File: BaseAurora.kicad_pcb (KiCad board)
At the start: 2 copper layers, 69.5 x 100 mm, 42 parts, among them J1 Conn_01x04_Male, J10 Conn_01x03_Male, J11 Screw_Terminal_01x02, J2 Conn_01x05_Male, J3 Screw_Terminal_01x02, J4 Conn_01x04_Male, J5 Conn_01x04_Male, J6 Screw_Terminal_01x02, J7 Screw_Terminal_01x02, J8 Header_1x2, J9 Header_1x2, K1 HK4100F-DC3V-SHG, Q1 2N3906, Q2 PN2222A, U1 ME6217C33M5G, U2 E32-915T20D, U3 4N32M, U4 NodeMCU1.0(ESP-12E)

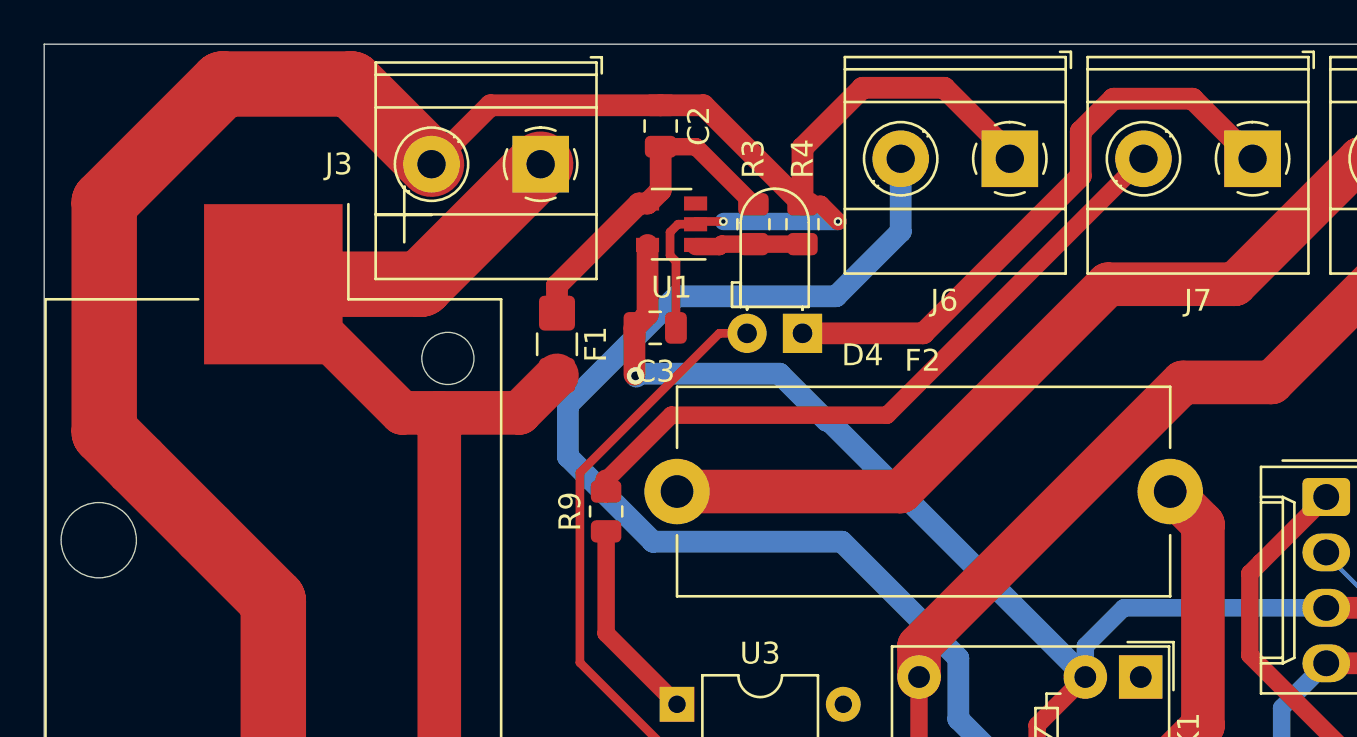
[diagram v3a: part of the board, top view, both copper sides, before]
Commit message: Adiciona CSV da BOM e vias de test points
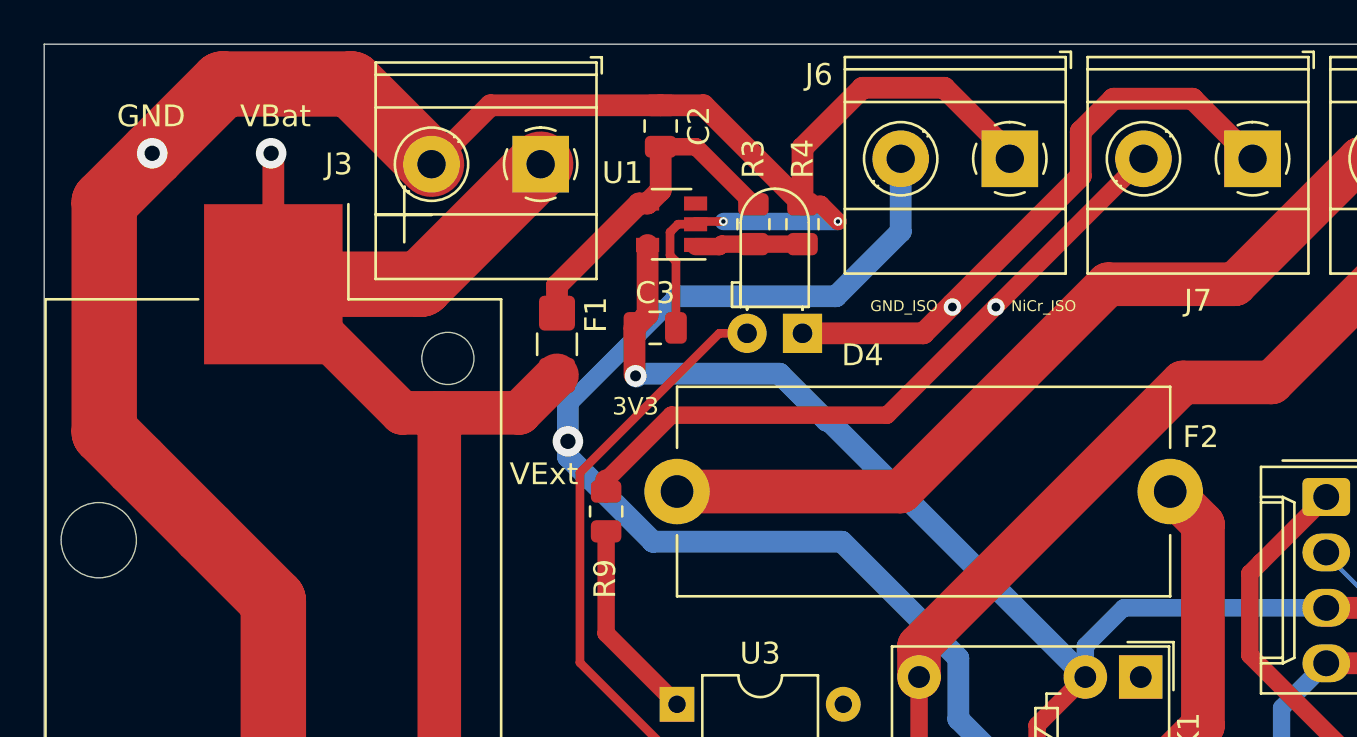
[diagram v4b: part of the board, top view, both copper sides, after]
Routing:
- net Vbat: track 78.9 -> 85.0 mm, vias 0 -> 1
- net Vext: vias 0 -> 1
- net GND_ISO: vias 0 -> 1
- net NiCr_ISO: vias 0 -> 1
- net GND: vias 4 -> 5
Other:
- board text added: "3V3"
- board text added: "GND"
- board text added: "GND_ISO"
- board text added: "NiCr_ISO"
- board text added: "VBat"
- board text added: "VExt"
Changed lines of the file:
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@@
   (general
     (thickness 1.6)
-    (drawings 8)
-    (tracks 374)
+    (drawings 14)
+    (tracks 385)
     (zones 0)
     (modules 42)
@@
     (tags SOT-23-5)
     (attr smd)
-    (fp_text reference U1 (at 0 -2.9) (layer F.SilkS)
+    (fp_text reference U1 (at 2.25 2.35) (layer F.SilkS)
       (effects (font (size 1 1) (thickness 0.15)))
     )
@@
     (descr https://www.tme.eu/en/Document/3b48dbe2b9714a62652c97b08fcd464b/PTF78.pdf)
     (tags "Fuseholder horizontal open 5x20 Stelvio-Kontek PTF/78")
-    (fp_text reference F2 (at 11.25 -6) (layer F.SilkS)
+    (fp_text reference F2 (at 24 -2.5) (layer F.SilkS)
       (effects (font (size 1 1) (thickness 0.15)))
     )
@@
     (tags "fuse castellated")
     (attr smd)
-    (fp_text reference F1 (at 0 -1.78 90) (layer F.SilkS)
+    (fp_text reference F1 (at -1.35 -1.78 90) (layer F.SilkS)
       (effects (font (size 1 1) (thickness 0.15)))
     )
@@
     (tags capacitor)
     (attr smd)
-    (fp_text reference C3 (at 0 2) (layer F.SilkS)
+    (fp_text reference C3 (at 0 -1.6) (layer F.SilkS)
       (effects (font (size 1 1) (thickness 0.15)))
     )
@@
     (descr "Terminal Block Phoenix MKDS-1,5-2, 2 pins, pitch 5mm, size 10x9.8mm^2, drill diamater 1.3mm, pad diameter 2.6mm, see http://www.farnell.com/datasheets/100425.pdf, script-generated using https://github.com/pointhi/kicad-footprint-generator/scripts/TerminalBlock_Phoenix")
     (tags "THT Terminal Block Phoenix MKDS-1,5-2 pitch 5mm size 10x9.8mm^2 drill 1.3mm pad 2.6mm")
-    (fp_text reference J6 (at 3 -6.5) (layer F.SilkS)
+    (fp_text reference J6 (at 8.75 3.85) (layer F.SilkS)
       (effects (font (size 1 1) (thickness 0.15)))
     )
@@
     (tags resistor)
     (attr smd)
-    (fp_text reference R9 (at 0 -1.65 90) (layer F.SilkS)
+    (fp_text reference R9 (at -3.0875 -0.05 90) (layer F.SilkS)
       (effects (font (size 1 1) (thickness 0.15)))
     )
@@
     )
   )
+  (gr_text VExt (at 214.4 41.95) (layer F.SilkS)
+    (effects (font (size 1 1) (thickness 0.15)))
+  )
+  (gr_text 3V3 (at 218.6 38.85) (layer F.SilkS)
+    (effects (font (size 0.8 0.8) (thickness 0.15)))
+  )
+  (gr_text NiCr_ISO (at 237.3 34.25) (layer F.SilkS)
+    (effects (font (size 0.5 0.5) (thickness 0.125)))
+  )
+  (gr_text GND_ISO (at 230.9 34.25) (layer F.SilkS)
+    (effects (font (size 0.5 0.5) (thickness 0.125)))
+  )
+  (gr_text VBat (at 202.1 25.55) (layer F.SilkS)
+    (effects (font (size 1 1) (thickness 0.15)))
+  )
+  (gr_text GND (at 196.4 25.55) (layer F.SilkS)
+    (effects (font (size 1 1) (thickness 0.15)))
+  )
   (dimension 100 (width 0.15) (layer Dwgs.User)
     (gr_text "100,000 mm" (at 174.95 72.25 270) (layer Dwgs.User)
@@
   (gr_line (start 261 22.25) (end 191.5 22.25) (layer Edge.Cuts) (width 0.05))
   (gr_line (start 261 122.25) (end 261 22.25) (layer Edge.Cuts) (width 0.05))
+  (via (at 201.9 27.25) (size 1.4) (drill 0.7) (layers F.Cu B.Cu) (net 2))
   (via (at 245.9 67.75) (size 0.8) (drill 0.4) (layers F.Cu B.Cu) (net 1))
   (via (at 229.5 67.25) (size 0.4) (drill 0.2) (layers F.Cu B.Cu) (net 1))
@@
   (segment (start 209.25 27.75) (end 205.57501 24.07501) (width 3) (layer F.Cu) (net 1))
   (segment (start 205.57501 24.07501) (end 199.67499 24.07501) (width 3) (layer F.Cu) (net 1))
-  (segment (start 199.67499 24.07501) (end 194.25 29.5) (width 3) (layer F.Cu) (net 1))
+  (segment (start 199.67499 24.07501) (end 196.45 27.3) (width 3) (layer F.Cu) (net 1))
   (segment (start 194.25 40.012998) (end 195.743501 41.506499) (width 3) (layer F.Cu) (net 1))
   (segment (start 221.7125 25.05) (end 226.25 29.5875) (width 1) (layer F.Cu) (net 1))
@@
   (segment (start 242.25 64.095029) (end 245.904971 67.75) (width 0.8) (layer B.Cu) (net 1))
   (segment (start 242.25 62.5) (end 242.25 64.095029) (width 0.8) (layer B.Cu) (net 1))
+  (segment (start 196.45 27.3) (end 194.25 29.5) (width 3) (layer F.Cu) (net 1))
+  (via (at 196.45 27.25) (size 1.4) (drill 0.7) (layers F.Cu B.Cu) (net 1))
   (segment (start 208.75 33.25) (end 202 33.25) (width 3) (layer F.Cu) (net 2))
   (segment (start 214.25 27.75) (end 208.75 33.25) (width 3) (layer F.Cu) (net 2))
@@
   (segment (start 207.895001 39.145001) (end 202 33.25) (width 2) (layer F.Cu) (net 2))
   (segment (start 215 37.425) (end 213.279999 39.145001) (width 2) (layer F.Cu) (net 2))
+  (segment (start 202 27.35) (end 201.9 27.25) (width 1) (layer F.Cu) (net 2))
+  (segment (start 202 33.25) (end 202 27.35) (width 1) (layer F.Cu) (net 2))
   (segment (start 227.2775 69) (end 229.3 69) (width 0.6) (layer F.Cu) (net 3) (status 30))
   (segment (start 227.2775 69) (end 227.2775 72.7225) (width 1) (layer F.Cu) (net 3))
@@
   (segment (start 221.3625 26.95) (end 219.75 26.95) (width 0.8) (layer F.Cu) (net 4))
   (segment (start 224 29.5875) (end 221.3625 26.95) (width 0.8) (layer F.Cu) (net 4))
-  (via (at 218.6 37.45) (size 0.8) (drill 0.4) (layers F.Cu B.Cu) (net 5))
+  (via (at 218.6 37.45) (size 1) (drill 0.5) (layers F.Cu B.Cu) (net 5))
   (segment (start 216.25 64.25) (end 223.69 64.25) (width 0.8) (layer F.Cu) (net 5) (status 30))
   (segment (start 223.69 64.25) (end 224.25 64.25) (width 0.6) (layer F.Cu) (net 5) (status 30))
@@
   (segment (start 223.71 35.5) (end 222.437208 35.5) (width 0.4) (layer F.Cu) (net 8))
   (segment (start 226.25 35.5) (end 226.5 35.25) (width 1) (layer F.Cu) (net 9))
-  (segment (start 231.790002 35.5) (end 239 28.290002) (width 1) (layer F.Cu) (net 9))
+  (segment (start 231.790002 35.5) (end 233.120001 34.170001) (width 1) (layer F.Cu) (net 9))
   (segment (start 226.25 35.5) (end 231.790002 35.5) (width 1) (layer F.Cu) (net 9))
   (segment (start 239 28.290002) (end 239 26.25) (width 1) (layer F.Cu) (net 9))
@@
   (segment (start 244.125 24.75) (end 246.875 27.5) (width 1) (layer F.Cu) (net 9))
   (segment (start 240.5 24.75) (end 244.125 24.75) (width 1) (layer F.Cu) (net 9))
+  (segment (start 233.120001 34.170001) (end 239 28.290002) (width 1) (layer F.Cu) (net 9))
+  (via (at 233.120001 34.29625) (size 0.8) (drill 0.4) (layers F.Cu B.Cu) (net 9))
   (segment (start 239.61 62.4) (end 239.71 62.5) (width 0.8) (layer F.Cu) (net 10))
   (segment (start 237 62.4) (end 239.61 62.4) (width 0.8) (layer F.Cu) (net 10))
@@
   (segment (start 230.75 30.84) (end 230.75 27.5) (width 1) (layer B.Cu) (net 25))
   (segment (start 227.790001 33.799999) (end 230.75 30.84) (width 1) (layer B.Cu) (net 25))
-  (segment (start 215.499999 38.779999) (end 220.479999 33.799999) (width 1) (layer B.Cu) (net 25))
+  (segment (start 215.499999 38.779999) (end 220.479999 33.799999) (width 0.8) (layer B.Cu) (net 25))
   (segment (start 240.785649 58.130001) (end 238.345999 58.130001) (width 1) (layer B.Cu) (net 25))
   (segment (start 247.004981 64.349333) (end 240.785649 58.130001) (width 0.8) (layer B.Cu) (net 25))
@@
   (segment (start 233.390001 50.385999) (end 228.054003 45.050001) (width 1) (layer B.Cu) (net 25))
   (segment (start 228.054003 45.050001) (end 219.395999 45.050001) (width 1) (layer B.Cu) (net 25))
-  (segment (start 215.499999 41.154001) (end 215.499999 38.779999) (width 1) (layer B.Cu) (net 25))
+  (segment (start 215.499999 41.154001) (end 215.499999 40.450001) (width 1) (layer B.Cu) (net 25))
   (segment (start 219.395999 45.050001) (end 215.499999 41.154001) (width 1) (layer B.Cu) (net 25))
   (segment (start 248.08 65.424352) (end 247.004981 64.349333) (width 0.8) (layer B.Cu) (net 25))
   (segment (start 248.08 69.75) (end 248.08 65.424352) (width 0.8) (layer B.Cu) (net 25))
+  (segment (start 215.499999 40.450001) (end 215.499999 38.779999) (width 1) (layer B.Cu) (net 25))
+  (via (at 215.499999 40.450001) (size 1.4) (drill 0.7) (layers F.Cu B.Cu) (net 25))
   (segment (start 245.33 69.96) (end 245.54 69.75) (width 0.8) (layer F.Cu) (net 26))
   (segment (start 245.33 74.75) (end 245.33 69.96) (width 0.8) (layer F.Cu) (net 26))
@@
   (segment (start 217.25 42.2375) (end 220.2375 39.25) (width 0.8) (layer F.Cu) (net 50))
   (segment (start 217.25 42.75) (end 217.25 42.2375) (width 1) (layer F.Cu) (net 50))
-  (segment (start 230.125 39.25) (end 241.875 27.5) (width 0.8) (layer F.Cu) (net 50))
+  (segment (start 230.125 39.25) (end 235.1125 34.2625) (width 0.8) (layer F.Cu) (net 50))
   (segment (start 220.2375 39.25) (end 230.125 39.25) (width 0.8) (layer F.Cu) (net 50))
+  (segment (start 235.1125 34.2625) (end 241.875 27.5) (width 0.8) (layer F.Cu) (net 50))
+  (via (at 235.1125 34.29625) (size 0.8) (drill 0.4) (layers F.Cu B.Cu) (net 50))
   (segment (start 231.59 56.33) (end 231.59 51.25) (width 0.8) (layer F.Cu) (net 51))
   (segment (start 231.59 49.835787) (end 243.675787 37.75) (width 2) (layer F.Cu) (net 51))

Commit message: Arquivos finais para fabricação
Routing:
- added copper zone on B.Cu, net GND
- added copper zone on F.Cu, net GND
